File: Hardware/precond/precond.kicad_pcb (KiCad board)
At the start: 2 copper layers, 40 parts, among them J1 Conn_Coaxial, J2 Conn_Coaxial, J3 Buck_logic_in, J4 3.3V_header, J5 XADC_headder, J6 Pmod_to_UART, Q1 IRLML6344TRPBF, Q2 IRLML9301TRPBF, U1 OPA2340, U2 OPA2340

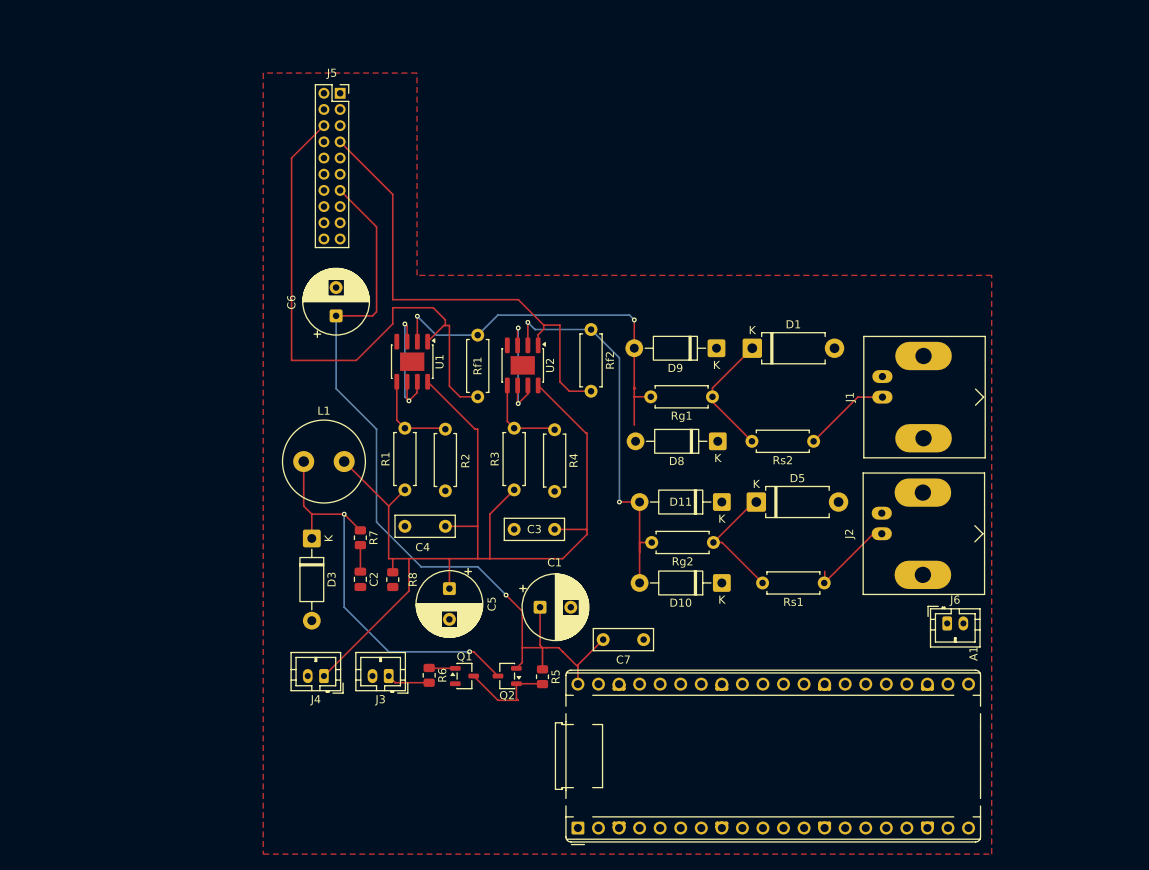
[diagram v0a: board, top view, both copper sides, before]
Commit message: PCB schematic changes
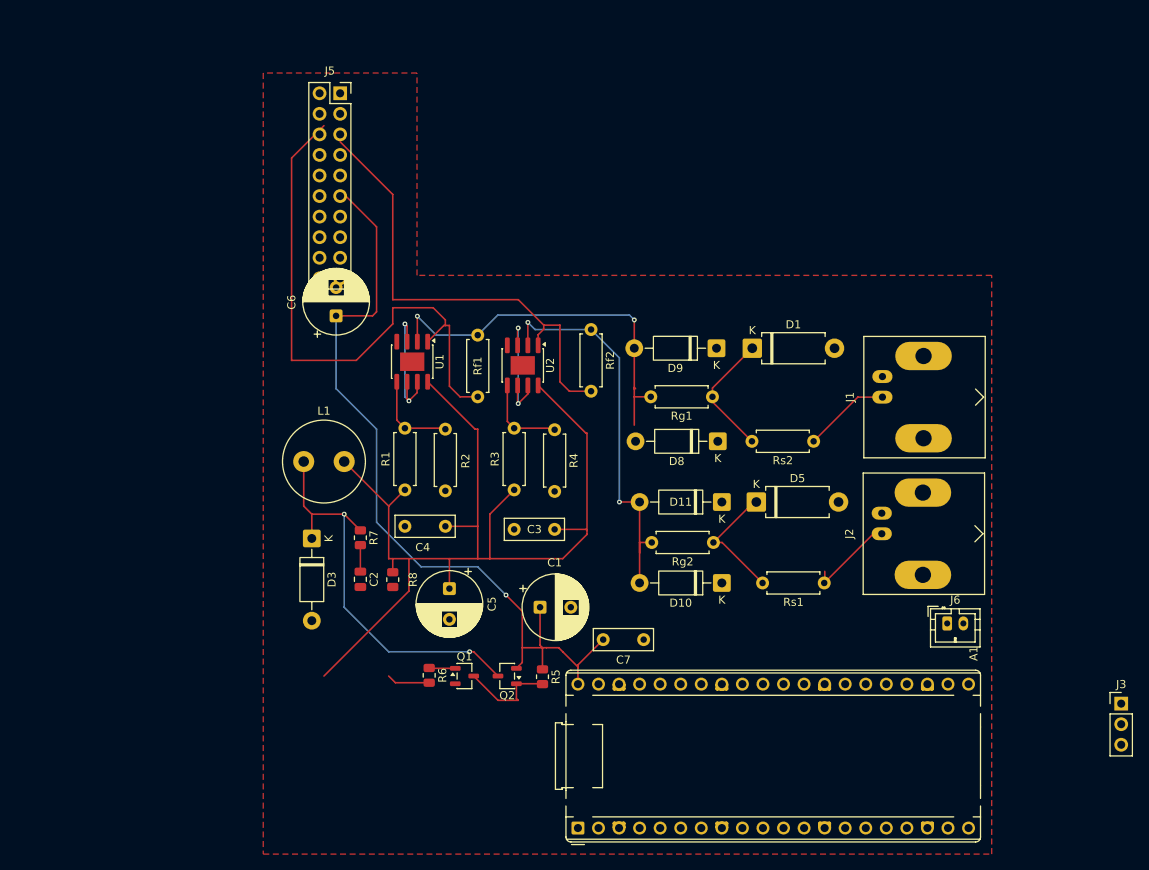
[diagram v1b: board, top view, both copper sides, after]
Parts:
- removed J4: 3.3V_header, Connector_JST:JST_PH_B2B-PH-K_1x02_P2.00mm_Vertical
- J3: value Buck_logic_in -> Screw_Terminal_01x03; footprint Connector_JST:JST_PH_B2B-PH-K_1x02_P2.00mm_Vertical -> Connector_PinHeader_2.54mm:PinHeader_1x03_P2.54mm_Vertical
- J5: footprint Connector_PinSocket_2.00mm:PinSocket_2x10_P2.00mm_Vertical -> Connector_PinSocket_2.54mm:PinSocket_2x10_P2.54mm_Vertical
- moved J3 90.6 mm to (156.5, 104.9), turned to 0 degrees
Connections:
- J3 pad 1: Net-(J3-Pin_1) -> GND
- J3 pad 2: unconnected-(J3-Pin_2-Pad2) -> +3.3V
- R6 pad 2: Net-(J3-Pin_1) -> Net-(J3-Pin_3)
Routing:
- net Net-(J3-Pin_3): track 0.00 -> 5.34 mm
- net Net-(J3-Pin_1): track 5.34 -> 0.00 mm

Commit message: no
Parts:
- removed the C6 at (59.5, 57.0)
- removed the C7 at (97.5, 97.0)
- removed J6: Pmod_to_UART, Connector_JST:JST_PH_B2B-PH-K_1x02_P2.00mm_Vertical
- added C2: 100n, Capacitor_THT:C_Rect_L7.2mm_W2.5mm_P5.00mm_FKS2_FKP2_MKS2_MKP2, F.Cu at (22.8, 107.5)
- added C4: 47uF, Capacitor_THT:CP_Radial_D8.0mm_P3.50mm, F.Cu at (57.5, 81.5)
- added C8: 100n, Capacitor_THT:C_Rect_L7.2mm_W2.5mm_P5.00mm_FKS2_FKP2_MKS2_MKP2, F.Cu at (75.5, 97.5)
- added C9: 100n, Capacitor_THT:C_Rect_L7.2mm_W2.5mm_P5.00mm_FKS2_FKP2_MKS2_MKP2, F.Cu at (67.0, 65.5)
- added H1: MountingHole, MountingHole:MountingHole_3.2mm_M3, F.Cu at (59.0, 109.5)
- added J4: Screw_Terminal_01x03, TerminalBlock_MetzConnect:TerminalBlock_MetzConnect_Type011_RT05503HBLC_1x03_P5.00mm_Horizontal, F.Cu at (106.8, 95.0)
- added TP1: TestPoint, TestPoint:TestPoint_Pad_2.5x2.5mm, F.Cu at (100.5, 75.0)
- added TP2: TestPoint, TestPoint:TestPoint_Pad_2.5x2.5mm, F.Cu at (78.2, 66.5)
- added TP3: TestPoint, TestPoint:TestPoint_Pad_2.5x2.5mm, F.Cu at (65.0, 99.0)
- added TP4: TestPoint, TestPoint:TestPoint_Pad_2.5x2.5mm, F.Cu at (85.0, 107.5)
- added TP5: TestPoint, TestPoint:TestPoint_Pad_2.5x2.5mm, F.Cu at (87.0, 61.5)
- J3: value Screw_Terminal_01x03 -> XADC_header; footprint Connector_PinHeader_2.54mm:PinHeader_1x03_P2.54mm_Vertical -> Connector_PinSocket_2.00mm:PinSocket_2x10_P2.00mm_Vertical; moved to B.Cu
- J5: value XADC_headder -> UART_hdr; footprint Connector_PinSocket_2.54mm:PinSocket_2x10_P2.54mm_Vertical -> Connector_JST:JST_PH_B3B-PH-K_1x03_P2.00mm_Vertical
- R7: footprint Resistor_SMD:R_0805_2012Metric -> Resistor_SMD:R_2512_6332Metric
- moved J3 156.9 mm to (23.0, 22.5), turned to 180 degrees
- moved R5 47.7 mm to (105.6, 68.5), turned to 0 degrees
- moved D2 45.8 mm to (75.6, 108.5), turned to 180 degrees
- moved J5 45.1 mm to (25.5, 58.6), turned to 90 degrees
- moved A1 45.1 mm to (45.0, 112.3), turned to 180 degrees
- moved Rf2 45.0 mm to (75.8, 101.0), turned to 180 degrees
- moved D5 44.7 mm to (64.9, 104.5), turned to 0 degrees
- moved J2 41.4 mm to (92.0, 106.1)
- moved Q1 40.6 mm to (99.0, 68.5), turned to 180 degrees
- moved Rs2 39.5 mm to (86.6, 111.5)
- moved D3 38.9 mm to (70.0, 59.6), turned to 90 degrees
- moved L1 37.3 mm to (92.5, 79.5), turned to -90 degrees
- moved J1 36.6 mm to (91.9, 56.6)
- moved Rg2 36.0 mm to (79.0, 108.6), turned to 90 degrees
- moved Rs1 34.9 mm to (87.2, 57.0), turned to 90 degrees
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- renumbered C3 to C1, C4 to C3, C1 to C5, C2 to C6, C5 to C7, D5 to D2, D8 to D3, D9 to D4, D10 to D5, D11 to D6, D3 to D7, R6 to R5, R5 to R6, Rs2 to Rs1, Rs1 to Rs2
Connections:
- A1 pad 13: GND -> AGND
- A1 pad 18: GND -> AGND
- A1 pad 23: GND -> AGND
- A1 pad 28: GND -> AGND
- A1 pad 3: GND -> AGND
- A1 pad 33: GND -> AGND
- A1 pad 38: GND -> AGND
- A1 pad 8: GND -> AGND
- C1 pad 2: GND -> AGND
- C3 pad 2: GND -> AGND
- C5 pad 2: GND -> AGND
- C6 pad 2: GND -> AGND
- C7 pad 2: GND -> AGND
- D1 pad 2: GND -> AGND
- D2 pad 2: GND -> AGND
- D3 pad 1: GND -> Net-(D3-K)
- D3 pad 2: Net-(D8-A) -> AGND
- D4 pad 1: GND -> +3.3V
- D4 pad 2: Net-(D8-A) -> Net-(D3-K)
- D5 pad 1: GND -> AGND
- D6 pad 1: GND -> +3.3V
- D7 pad 2: GND -> AGND
- J1 pad 2: GND -> AGND
- J2 pad 2: GND -> AGND
- J3 pad 1: GND -> AGND
- J3 pad 2: +3.3V -> /Op1_out
- J3 pad 3: Net-(J3-Pin_3) -> AGND
- J5 pad 1: unconnected-(J5-Pin_1-Pad1) -> AGND
- J5 pad 2: unconnected-(J5-Pin_2-Pad2) -> Net-(A1-GPIO17)
- J5 pad 3: GND -> Net-(A1-GPIO16)
- Q1 pad 2: GND -> AGND
- R2 pad 2: GND -> AGND
- R4 pad 2: GND -> AGND
- R5 pad 2: Net-(J3-Pin_3) -> Net-(J4-Pin_3)
- R8 pad 2: GND -> AGND
- Rf1 pad 1: Net-(D8-A) -> Net-(D3-K)
- Rg1 pad 2: Net-(D8-A) -> Net-(D3-K)
- U1 pad 2: Net-(D8-A) -> Net-(D3-K)
- U1 pad 4: GND -> AGND
- U2 pad 4: GND -> AGND
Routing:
- net +5V: track 102.1 -> 180.4 mm, vias 1 -> 2
- net /Op2_out: track 58.3 -> 106.3 mm, vias 0 -> 1
- net Net-(D8-A): track 47.2 -> 0.00 mm, vias 2 -> 0
- net Net-(D7-K): track 50.8 -> 23.2 mm
- net Net-(D5-A): track 48.6 -> 24.3 mm, vias 2 -> 0
- net /Op1_out: track 69.9 -> 92.7 mm
- net Net-(D3-K): track 0.00 -> 20.4 mm
- net +3.3V: track 130.5 -> 150.6 mm, vias 0 -> 3
- net Net-(J4-Pin_3): track 0.00 -> 16.6 mm
- net Net-(A1-GPIO17): track 0.00 -> 11.6 mm
- net Net-(A1-GPIO16): track 0.00 -> 10.1 mm
- net Net-(D2-A1): track 15.5 -> 6.35 mm
- net Net-(Q1-Pad3): track 12.1 -> 4.30 mm
- net AGND: track 0.00 -> 6.63 mm, vias 0 -> 19
- net Net-(D1-A1): track 15.6 -> 9.16 mm
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- added copper zone on B.Cu, net AGND
- added copper zone on F.Cu, net AGND
- removed copper zone on F.Cu, net GND
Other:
- board outline added: 92 x 96 mm
- board text added: "AK GJ LS VM YP (C) 2026"
- board text added: "H1"
- board text added: "Preconditionificator 9000"
- board text added: "perry the platypus"

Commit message: finished?
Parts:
- J5: footprint Connector_JST:JST_PH_B3B-PH-K_1x03_P2.00mm_Vertical -> Connector_PinHeader_2.54mm:PinHeader_1x03_P2.54mm_Vertical
- moved J3 18.1 mm to (25.0, 40.5), turned to 0 degrees
- moved J1 7.07 mm to (98.9, 55.6)
- moved J2 7.07 mm to (99.0, 107.1)
- moved J5 0.69 mm to (25.0, 59.1), turned to 180 degrees
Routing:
- net /Op1_out: track 92.7 -> 79.8 mm
- net /Op2_out: track 106.3 -> 97.8 mm, vias 1 -> 2
- net Net-(J1-In): track 9.31 -> 16.9 mm
- net Net-(J2-In): track 12.3 -> 18.9 mm
- net AGND: track 6.63 -> 3.80 mm, vias 19 -> 91
- net Net-(A1-GPIO17): track 11.6 -> 14.0 mm
- net +5V: track 180.4 -> 181.0 mm, vias 2 -> 1
